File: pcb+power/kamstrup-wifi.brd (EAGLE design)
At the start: 36 x 81.3 mm, 26 parts, among them T1 BT137, T2 BT137, U1 ESP8266-07, U2 MCP1316T-29LE/OT

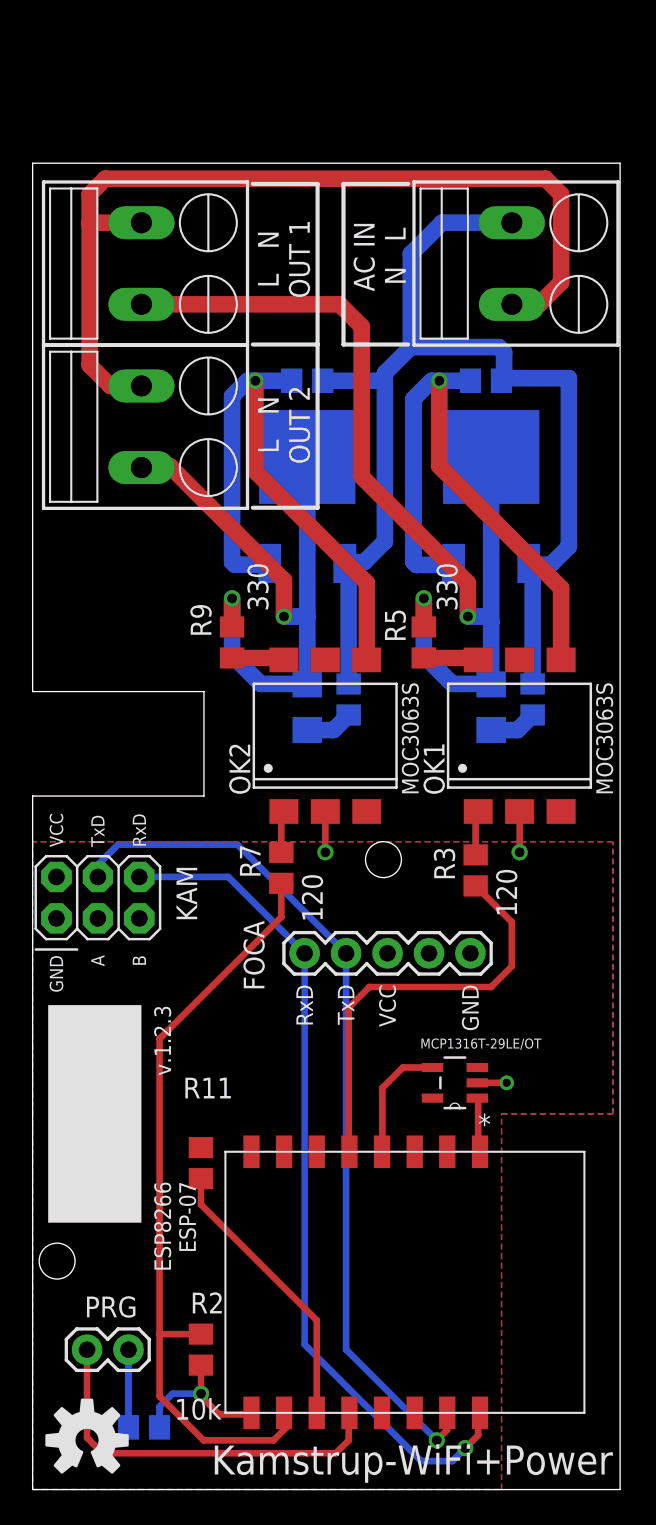
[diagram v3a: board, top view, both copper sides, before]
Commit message: pcb board made 8 mm higher for better fixation in kamstrup meter
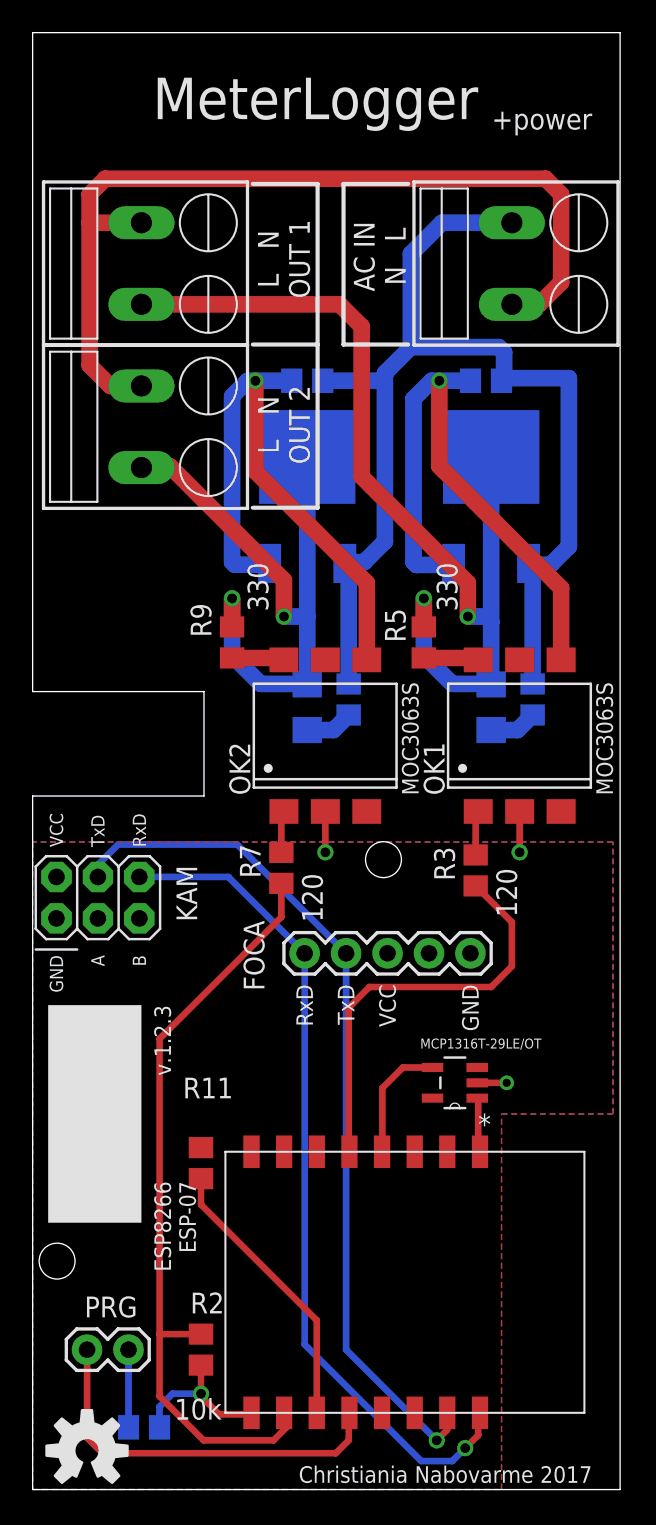
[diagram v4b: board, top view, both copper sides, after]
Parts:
- moved U$2 0.63 mm to (3.33, 2.38)
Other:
- board size 36 x 81.3 mm -> 36 x 89.3 mm
- board text added: "+power"
- board text added: "Christiania Nabovarme 2017"
- board text added: "MeterLogger"
- board text removed: "Kamstrup-WiFi+Power"
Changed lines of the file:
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@@
 <setting verticaltext="up"/>
 </settings>
-<grid distance="0.025" unitdist="inch" unit="inch" style="lines" multiple="1" display="no" altdistance="0.0025" altunitdist="inch" altunit="inch"/>
+<grid distance="0.025" unitdist="inch" unit="mm" style="lines" multiple="1" display="no" altdistance="0.0025" altunitdist="inch" altunit="mm"/>
 <layers>
 <layer number="1" name="Top" color="4" fill="1" visible="yes" active="yes"/>
@@
 <plain>
 <wire x1="0" y1="0" x2="36" y2="0" width="0" layer="20"/>
-<wire x1="36" y1="0" x2="36" y2="81.28" width="0" layer="20"/>
-<wire x1="36" y1="81.28" x2="0" y2="81.28" width="0" layer="20"/>
-<wire x1="0" y1="81.28" x2="0" y2="48.9" width="0" layer="20"/>
+<wire x1="36" y1="0" x2="36" y2="89.28" width="0" layer="20"/>
+<wire x1="36" y1="89.28" x2="0" y2="89.28" width="0" layer="20"/>
+<wire x1="0" y1="89.28" x2="0" y2="48.9" width="0" layer="20"/>
 <wire x1="0" y1="48.9" x2="10.5" y2="48.9" width="0" layer="20"/>
 <wire x1="10.5" y1="48.9" x2="10.5" y2="42.5" width="0" layer="20"/>
@@
 <wire x1="19.05" y1="70.1675" x2="23.01875" y2="70.1675" width="0.254" layer="25"/>
 <wire x1="19.05" y1="80.01" x2="19.05" y2="70.1675" width="0.254" layer="25"/>
-<text x="35.56" y="2.69875" size="1.778" layer="25" ratio="15" rot="R180">Kamstrup-WiFi+Power</text>
+<text x="27.305" y="83.97875" size="2.54" layer="25" ratio="15" rot="R180" align="top-left">MeterLogger</text>
 <rectangle x1="0.9525" y1="16.35125" x2="6.6675" y2="29.68625" layer="25"/>
 <text x="15.39875" y="75.40625" size="1.27" layer="25" ratio="20" rot="R270" align="center">L   N
@@
 <text x="15.39875" y="65.24625" size="1.27" layer="25" ratio="20" rot="R270" align="center">L   N
 OUT 2</text>
+<text x="34.29" y="1.42875" size="1.016" layer="25" ratio="15" rot="R180">Christiania Nabovarme 2017</text>
+<text x="34.29" y="83.34375" size="1.27" layer="25" ratio="15" rot="R180" align="top-left">+power</text>
 </plain>
 <attributes>
@@
 <attribute name="NAME" x="6.4262" y="11.8237" size="1.27" layer="25" ratio="10" rot="R180"/>
 </element>
-<element name="U$2" library="SparkFun-Aesthetics" package="OSHW-LOGO-M" value="" x="3.33375" y="3.01625"/>
+<element name="U$2" library="SparkFun-Aesthetics" package="OSHW-LOGO-M" value="" x="3.33375" y="2.38125"/>
 <element name="R1" library="rcl" package="R0805" value="10k" x="6.82625" y="3.81" smashed="yes" rot="MR0">
 <attribute name="NAME" x="8.73125" y="5.23875" size="1.27" layer="26" rot="MR0"/>
